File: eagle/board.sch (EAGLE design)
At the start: 26 parts, among them Q1 5MHz, U1 P8X32A-D40, U2 74LS138N, U3 74LS139N, U4 24C256

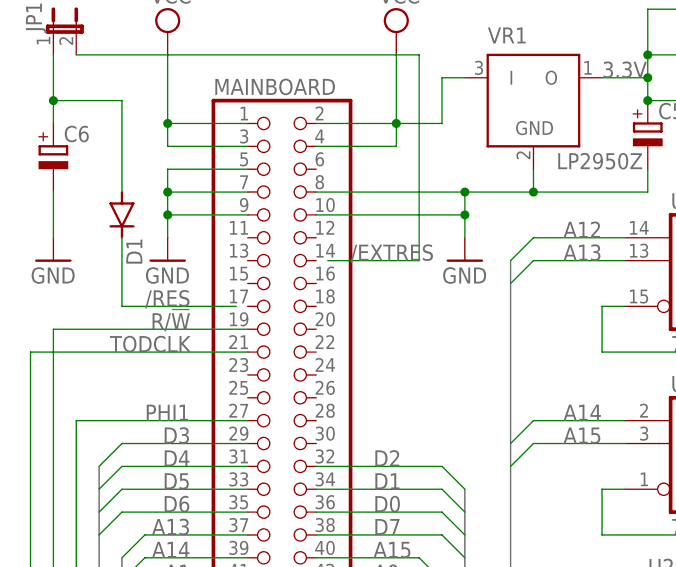
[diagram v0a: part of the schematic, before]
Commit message: Board and firmware fixes.
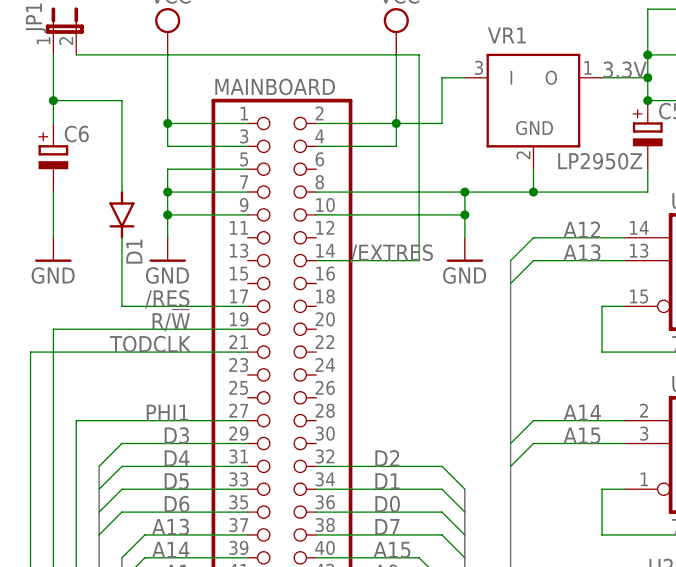
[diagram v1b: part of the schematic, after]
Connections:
- net /EXTRES: now also MAINBOARD.14
- net /RES: now also MAINBOARD.17
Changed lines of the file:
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@@
 <net name="/EXTRES" class="0">
 <segment>
-<wire x1="33.02" y1="76.2" x2="43.18" y2="76.2" width="0.1524" layer="91"/>
+<wire x1="31.75" y1="76.2" x2="43.18" y2="76.2" width="0.1524" layer="91"/>
 <wire x1="43.18" y1="76.2" x2="43.18" y2="99.06" width="0.1524" layer="91"/>
 <wire x1="43.18" y1="99.06" x2="5.08" y2="99.06" width="0.1524" layer="91"/>
 <label x="35.56" y="76.2" size="1.778" layer="95"/>
 <pinref part="JP1" gate="A" pin="2"/>
+<pinref part="MAINBOARD" gate="A" pin="14"/>
 </segment>
 </net>
@@
 <net name="/RES" class="0">
 <segment>
-<wire x1="22.86" y1="71.12" x2="10.16" y2="71.12" width="0.1524" layer="91"/>
+<wire x1="24.13" y1="71.12" x2="10.16" y2="71.12" width="0.1524" layer="91"/>
 <wire x1="10.16" y1="71.12" x2="10.16" y2="78.74" width="0.1524" layer="91"/>
 <pinref part="D1" gate="G$1" pin="C"/>
 <label x="17.78" y="71.12" size="1.778" layer="95" rot="MR0"/>
+<pinref part="MAINBOARD" gate="A" pin="17"/>
 </segment>
 </net>
